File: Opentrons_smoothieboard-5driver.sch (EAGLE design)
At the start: 385 parts, among them IC1 LPC1769, IC10 LM1117-3.3V, IC11 78L12F, IC12 A4982, IC13 R-78E-5.0, IC14 TC4427, IC15 TC4427, IC2 A4982, IC3 A4982, IC4 MCP44X1, IC5 A4982, IC6 A4982, IC9 MCP44X1, J10 POWER_JACKSMD, Q1 BSL207SP, Q10 SUD50P04-08-GE3, Q2 12MHz, Q3 25MHz, Q4 ZXMN4A06, Q5 AOT240L, Q6 AOT240L, Q7 AOT240L, Q8 ZXMN4A06, Q9 ZXMN4A06, U1 USD-SOCKETNEW, X14 USBPTH

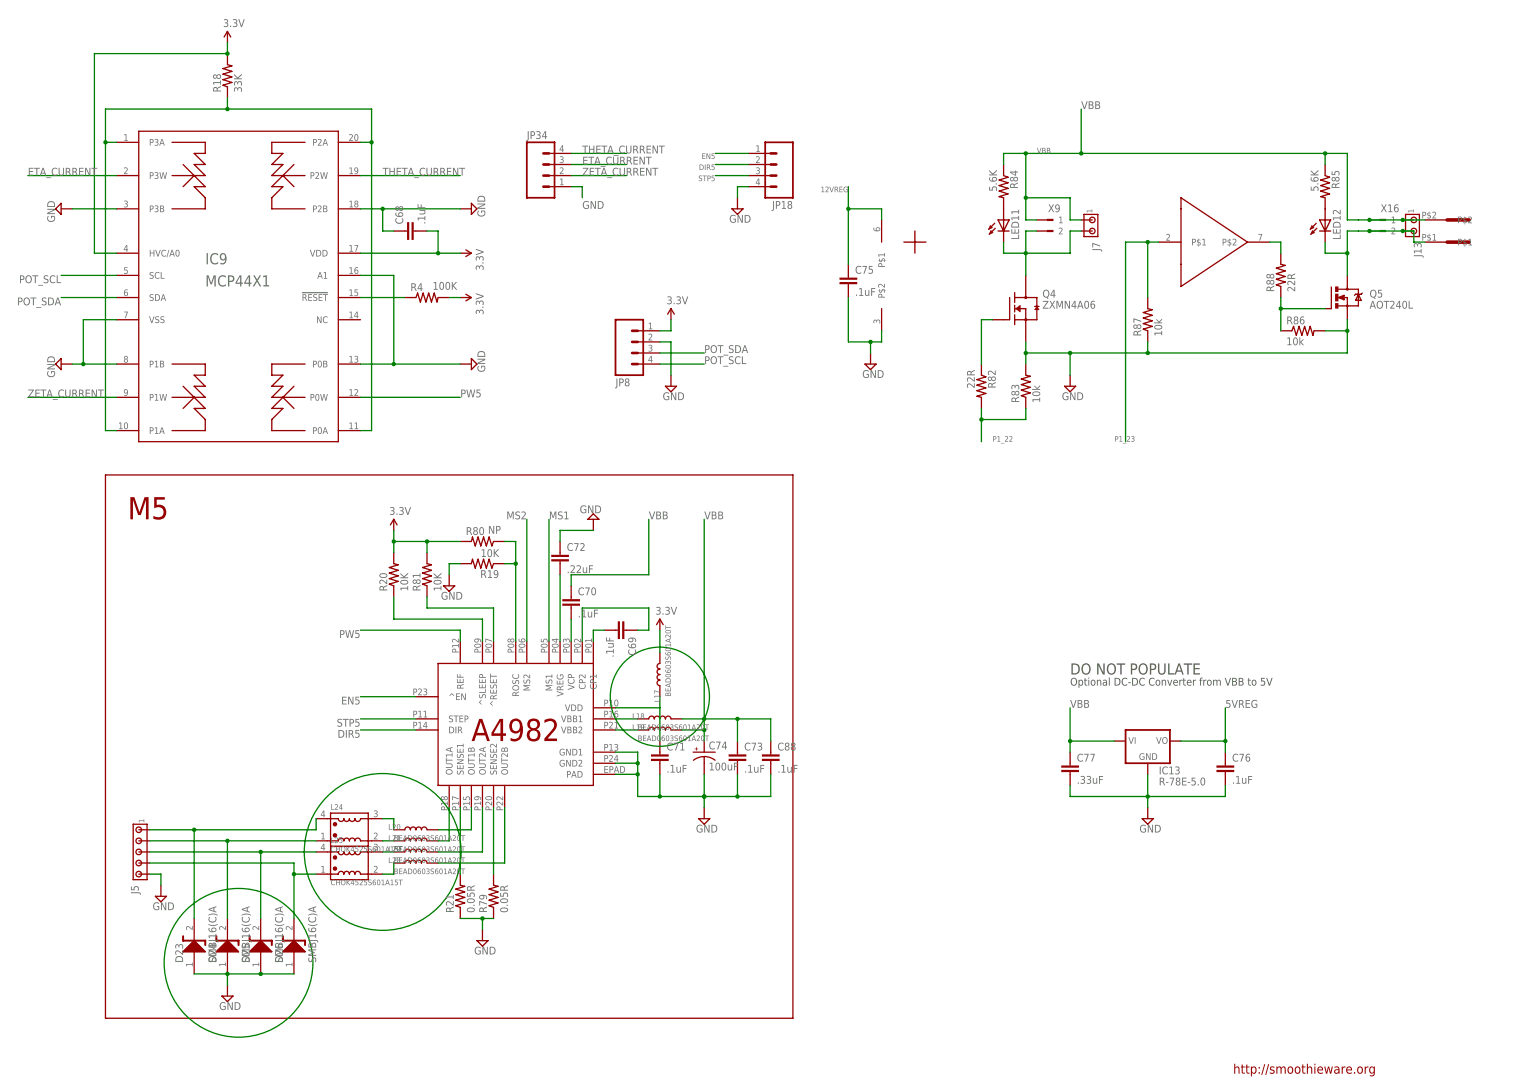
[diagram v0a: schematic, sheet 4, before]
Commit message: adds 6th driver
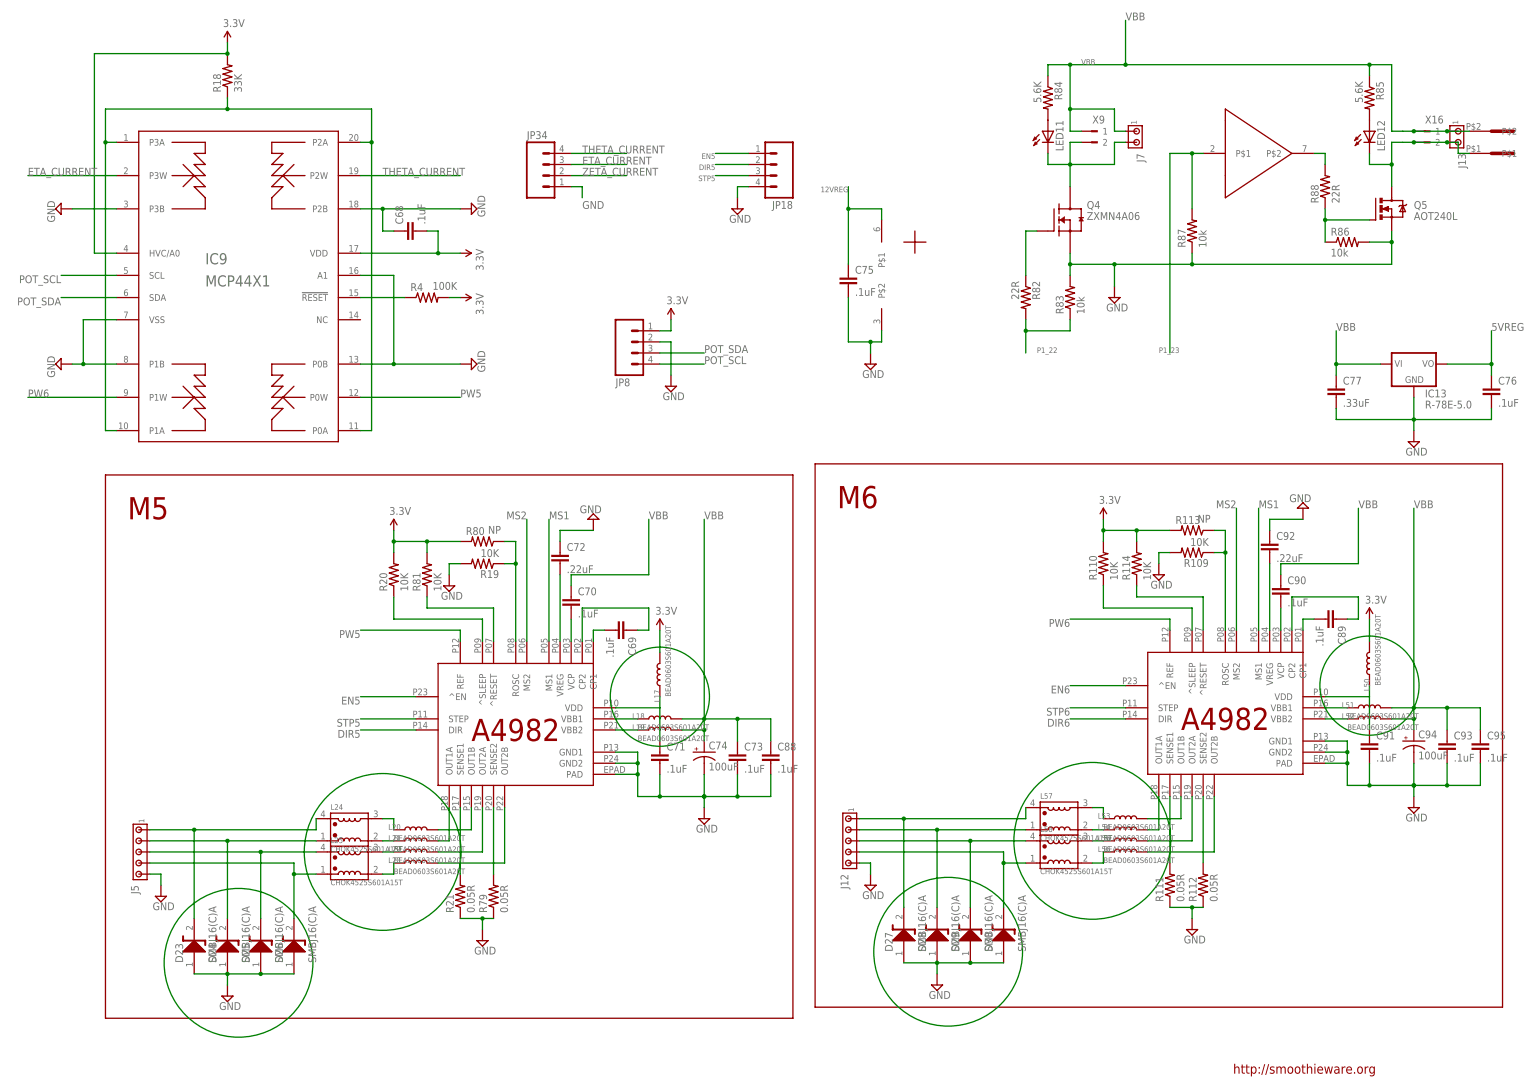
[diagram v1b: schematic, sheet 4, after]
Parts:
- added C89, C90, C91, C93, C95: .1uF, rcl:C-EUC0603
- added C92: .22uF, rcl:C-EUC0603
- added C94: 100uF, SparkFun:CAP_POLE
- added D27, D28, D29, D30: SMBJ16(C)A, My_Lib:SMBJ16(C)A
- added IC16: A4982, A4982:A4982
- added J12: (no value), con-amp:MTA05-100
- added L50, L51, L52, L53, L54, L55, L56: BEAD0603S601A20T, My_Lib:INDOUCTOR0603
- added L57, L58: CHOK4525S601A15T, My_Lib:CHOK-4525S-XXX
- added R109, R110, R114: 10K, resistor:R-US_R0603
- added R111, R112: 0.05R, SparkFun:RESISTOR2512
- added R113: NP, resistor:R-US_R0603
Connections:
- new net DIR6: IC16.DIR
- new net EN6: IC16.^EN
- new net J5_1A1: D27.K, J12.1, L57.4
- new net J5_1B1: D28.K, J12.2, L57.1
- new net J5_2A1: D29.K, J12.3, L58.4
- new net J5_2B1: D30.K, J12.4, L58.1
- new net N$11: C89.2, IC16.CP1
- new net N$120: C89.1, IC16.CP2
- new net N$169: C90.2, IC16.VCP
- new net N$178: IC16.SENSE1, R111.2
- new net N$179: IC16.SENSE2, R112.2
- new net N$180: IC16.OUT1A, L54.2
- new net N$181: IC16.OUT1B, L53.2
- new net N$184: IC16.OUT2A, L55.2
- new net N$185: IC16.OUT2B, L56.2
- new net N$186: IC16.ROSC, R109.1, R113.1
- new net N$187: C92.2, IC16.VREG
- new net N$188: IC16.^SLEEP, R110.1
- new net N$189: IC16.^RESET, R114.1
- new net N$190: C91.1, IC16.VDD, L50.1
- new net N$191: IC16.VBB1, L51.1
- new net N$192: IC16.VBB2, L52.1
- new net N$193: L54.1, L57.2
- new net N$194: L53.1, L57.3
- new net N$195: L55.1, L58.3
- new net N$196: L56.1, L58.2
- new net PW6: IC16.REF, IC9.P1W
- new net STP6: IC16.STEP
- net 3.3V: now also L50.2, R110.2, R113.2, R114.2
- net GND: now also C91.2, C92.1, C93.2, C94.-, C95.2, D27.A, D28.A, D29.A, D30.A, IC16.GND1, IC16.GND2, IC16.PAD, J12.5, R109.2, R111.1, R112.1
- net MS1: now also IC16.MS1
- net MS2: now also IC16.MS2
- net VBB: now also C90.1, C93.1, C94.+, C95.1, L51.2, L52.2
- net ZETA_CURRENT: no longer IC9.P1W
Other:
- note added: "M6"
- note removed: "DO NOT POPULATE"
- note removed: "Optional DC-DC Converter from VBB to 5V"
- moved on the sheet: C76, C77, IC13, J13, J7, LED11, LED12, Q4, Q5, R82, R83, R84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
